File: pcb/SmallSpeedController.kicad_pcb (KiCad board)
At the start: 4 copper layers, 30.7 x 51.7 mm, 38 parts, among them J1 Conn_01x02_Socket, J10 Conn_01x03_Socket, J11 Conn_01x03_Socket, J2 Conn_01x02_Socket, J4 Conn_01x02_Socket, J5 Conn_01x04_Socket, J6 Conn_01x04_Socket, J9 Conn_01x03_Socket, SW2 TS-1088-AR02016, U2 AMS1117-3.3, U3 DRV8837DSGR, U4 DRV8837DSGR, U5 CH32V003FxUx

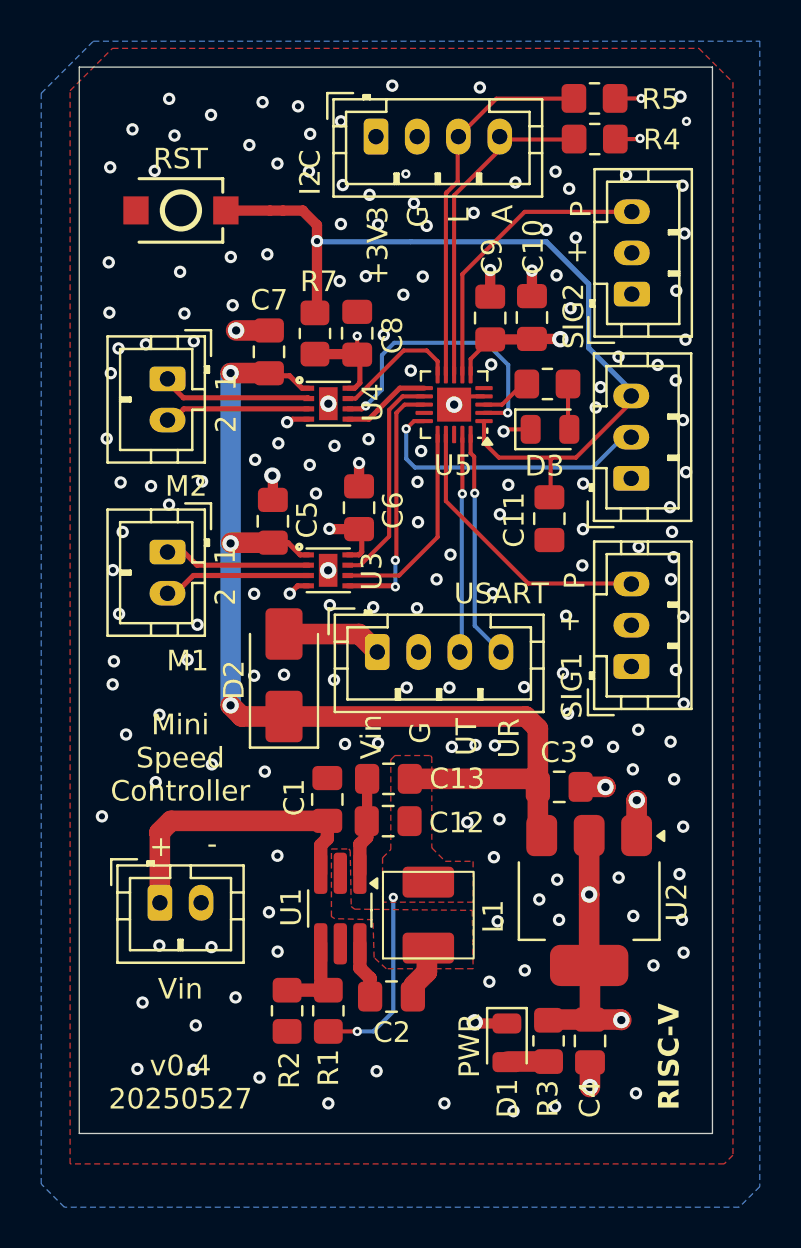
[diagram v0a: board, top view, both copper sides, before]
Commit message: pcb, sch: small cleanups for next fabrication round
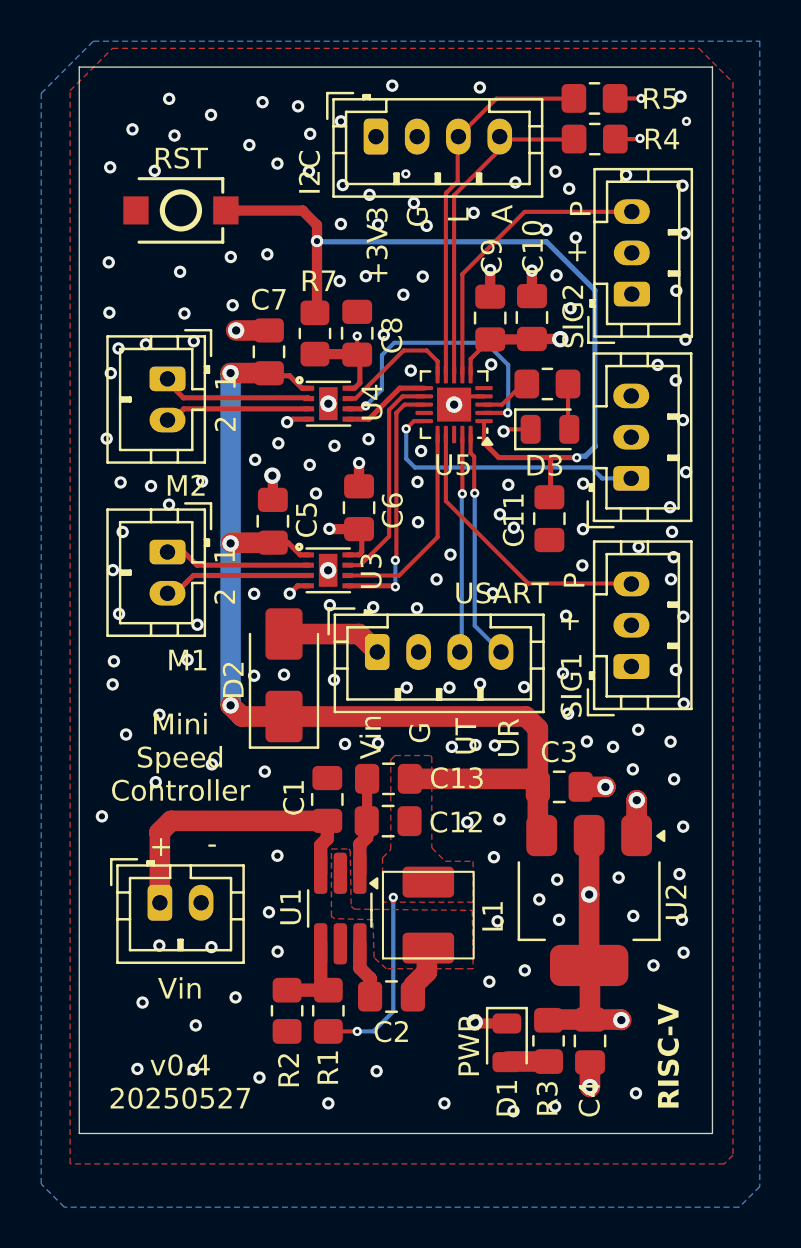
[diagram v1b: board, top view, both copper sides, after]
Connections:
- J11 pad 1: GND -> /SWDIO
- J11 pad 2: /SWDIO -> /+3V3
- J11 pad 3: /nRST -> GND
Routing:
- net /nRST: track 40.2 -> 39.3 mm, vias 1 -> 2
- net GND: vias 177 -> 176
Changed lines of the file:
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@@
 			(remove_unused_layers no)
 			(roundrect_rratio 0.208333)
-			(net 2 "GND")
+			(net 9 "/SWDIO")
 			(pinfunction "Pin_1")
 			(pintype "passive")
@@
 			(layers "*.Cu" "*.Mask")
 			(remove_unused_layers no)
-			(net 9 "/SWDIO")
+			(net 3 "/+3V3")
 			(pinfunction "Pin_2")
 			(pintype "passive")
@@
 			(layers "*.Cu" "*.Mask")
 			(remove_unused_layers no)
-			(net 4 "/nRST")
+			(net 2 "GND")
 			(pinfunction "Pin_3")
 			(pintype "passive")
@@
 	)
 	(via
-		(at 44.57 84.79)
-		(size 0.6)
-		(drill 0.3)
-		(layers "F.Cu" "B.Cu")
-		(free yes)
-		(net 2)
-	)
-	(via
 		(at 25.91 70.6)
 		(size 0.6)
@@
 	)
 	(via
+		(at 38.96 98.19)
+		(size 0.6)
+		(drill 0.3)
+		(layers "F.Cu" "B.Cu")
+		(free yes)
+		(net 2)
+	)
+	(via
 		(at 31.9 86.65)
 		(size 0.6)
@@
 	)
 	(via
-		(at 44.8 83.8)
+		(at 32.21 75.89)
 		(size 0.6)
 		(drill 0.3)
@@
 	)
 	(via
-		(at 32.21 75.89)
+		(at 21.02 73.14)
 		(size 0.6)
 		(drill 0.3)
@@
 	)
 	(via
-		(at 21.02 73.14)
+		(at 47.575 82.725)
 		(size 0.6)
 		(drill 0.3)
@@
 	)
 	(via
-		(at 47.575 82.725)
+		(at 40.6 90.62)
 		(size 0.6)
 		(drill 0.3)
@@
 	)
 	(via
-		(at 45.675 82.325)
-		(size 0.6)
-		(drill 0.3)
-		(layers "F.Cu" "B.Cu")
-		(free yes)
-		(net 2)
-	)
-	(via
 		(at 25.25 95.325)
 		(size 0.6)
@@
 	)
 	(segment
-		(start 43.61 87.22)
-		(end 46.205 84.625)
-		(width 0.2)
-		(layer "F.Cu")
-		(net 4)
-	)
-	(segment
 		(start 42.47 87.22)
 		(end 42.38 87.31)
@@
 		(start 39.15 86.5)
 		(end 39.87 87.22)
-		(width 0.2)
+		(width 0.25)
 		(layer "F.Cu")
 		(net 4)
 	)
 	(segment
-		(start 29.4 75.24)
-		(end 28.77 75.24)
+		(start 27.19 75.24)
+		(end 30.37 75.24)
 		(width 0.5)
 		(layer "F.Cu")
@@
 		(start 39.87 87.22)
 		(end 42.47 87.22)
-		(width 0.2)
+		(width 0.25)
 		(layer "F.Cu")
 		(net 4)
@@
 	)
 	(segment
-		(start 28.77 75.24)
-		(end 27.19 75.24)
-		(width 0.5)
-		(layer "F.Cu")
-		(net 4)
-	)
-	(segment
 		(start 42.38 87.31)
 		(end 42.38 89.1525)
-		(width 0.2)
+		(width 0.25)
 		(layer "F.Cu")
 		(net 4)
@@
 		(start 42.47 87.22)
 		(end 43.61 87.22)
-		(width 0.2)
+		(width 0.25)
 		(layer "F.Cu")
 		(net 4)
 	)
-	(segment
-		(start 30.37 75.24)
-		(end 29.4 75.24)
-		(width 0.5)
-		(layer "F.Cu")
+	(via
+		(at 43.65 87.225)
+		(size 0.45)
+		(drill 0.2)
+		(layers "F.Cu" "B.Cu")
 		(net 4)
 	)
@@
 	)
 	(segment
-		(start 46.525 84.2)
-		(end 44.225 81.9)
+		(start 44.07 87.15)
+		(end 44.55 86.67)
 		(width 0.25)
 		(layer "B.Cu")
@@
 	)
 	(segment
-		(start 31.08 76.75)
-		(end 35.6 76.75)
+		(start 43.725 87.15)
+		(end 44.07 87.15)
 		(width 0.25)
 		(layer "B.Cu")
@@
 	)
 	(segment
-		(start 44.225 81.9)
-		(end 44.225 78.8)
+		(start 44.53 86.65)
+		(end 44.53 79.105)
 		(width 0.25)
 		(layer "B.Cu")
@@
 	)
 	(segment
-		(start 44.225 78.8)
+		(start 43.65 87.225)
+		(end 43.725 87.15)
+		(width 0.25)
+		(layer "B.Cu")
+		(net 4)
+	)
+	(segment
+		(start 44.55 86.67)
+		(end 44.53 86.65)
+		(width 0.25)
+		(layer "B.Cu")
+		(net 4)
+	)
+	(segment
+		(start 44.53 79.105)
 		(end 42.175 76.75)
 		(width 0.25)
@@
 	(segment
 		(start 42.175 76.75)
-		(end 35.6 76.75)
+		(end 31.08 76.75)
 		(width 0.25)
 		(layer "B.Cu")
@@
 	)
 	(segment
-		(start 44.425 87.7)
-		(end 45.925 86.2)
+		(start 35.376 85.825)
+		(end 35.376 87.276)
 		(width 0.2)
 		(layer "B.Cu")
@@
 	)
 	(segment
-		(start 35.376 85.825)
-		(end 35.376 87.276)
+		(start 44.88 88.23)
+		(end 46.29 88.23)
 		(width 0.2)
 		(layer "B.Cu")
@@
 	)
 	(segment
-		(start 35.376 87.276)
-		(end 35.8 87.7)
+		(start 44.35 87.7)
+		(end 44.88 88.23)
 		(width 0.2)
 		(layer "B.Cu")
@@
 	(segment
 		(start 35.8 87.7)
-		(end 44.425 87.7)
+		(end 44.35 87.7)
+		(width 0.2)
+		(layer "B.Cu")
+		(net 9)
+	)
+	(segment
+		(start 35.376 87.276)
+		(end 35.8 87.7)
 		(width 0.2)
 		(layer "B.Cu")

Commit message: pcb: move silk prints around
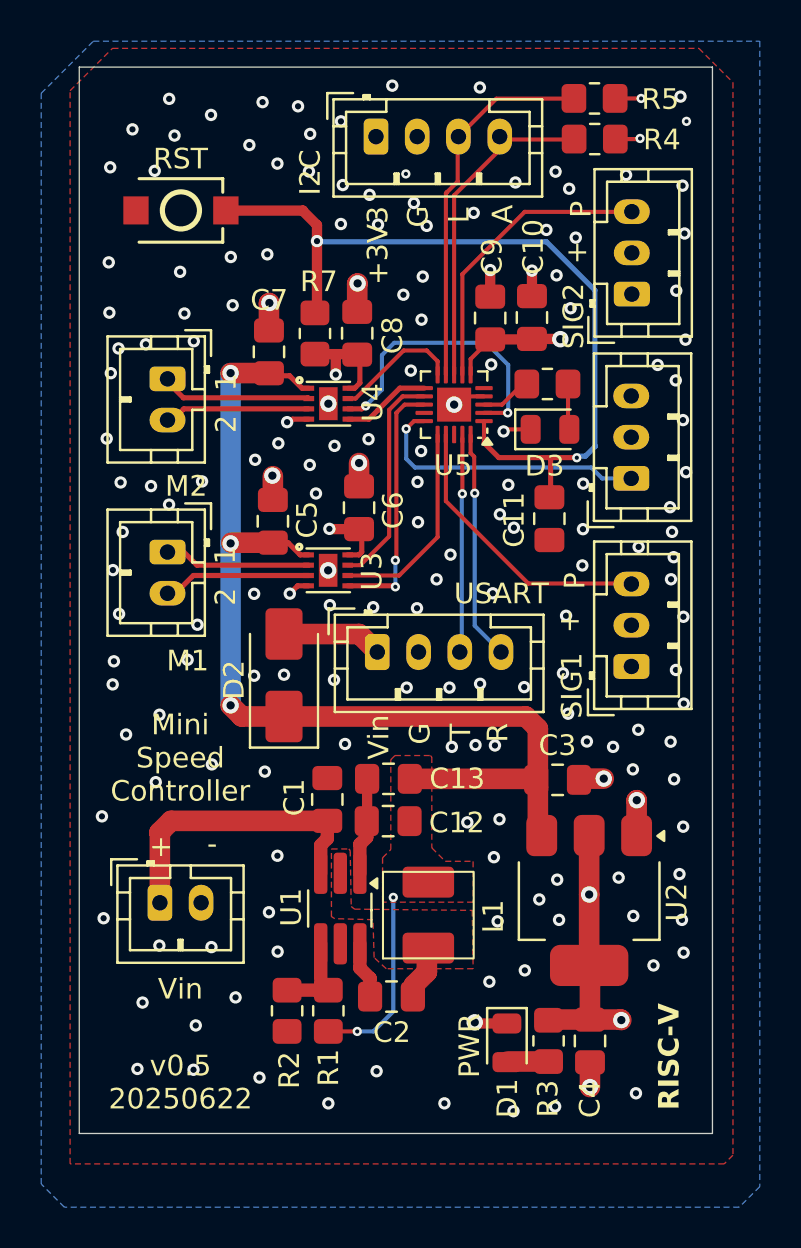
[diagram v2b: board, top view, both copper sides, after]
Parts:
- C11: value C -> 100nF
- U1: value ~ -> AP62300TWU
- moved C3 0.35 mm to (42.7, 102.8)
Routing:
- net GND: track 21.4 -> 22.5 mm, vias 176 -> 175
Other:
- board text added: "R"
- board text added: "T"
- board text added: "v0.5 20250622"
- board text removed: "UR"
- board text removed: "UT"
- board text removed: "v0.4 20250527"
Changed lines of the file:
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@@
 	(footprint "Capacitor_SMD:C_0805_2012Metric_Pad1.18x1.45mm_HandSolder"
 		(layer "F.Cu")
-		(at 42.8 103.19)
+		(at 42.72 102.85)
 		(descr "Capacitor SMD 0805 (2012 Metric), square (rectangular) end terminal, IPC-7351 nominal with elongated pad for handsoldering. (Body size source: IPC-SM-782 page 76, https://www.pcb-3d.com/wordpress/wp-content/uploads/ipc-sm-782a_amendment_1_and_2.pdf, https://docs.google.com/spreadsheets/d/1BsfQQcO9C6DZCsRaXUlFlo91Tg2WpOkGARC1WS5S8t0/edit?usp=sharing), generated with kicad-footprint-generator")
 		(tags "capacitor handsolder")
@@
 			)
 		)
-		(property "Value" "C"
+		(property "Value" "100nF"
 			(at 0 1.68 90)
 			(layer "F.Fab")
@@
 			)
 		)
-		(property "Value" "~"
+		(property "Value" "AP62300TWU"
 			(at 0 2.5 90)
 			(layer "F.Fab")
@@
 	)
 	(gr_text "G"
-		(at 36.65 101.1 90)
+		(at 36.63 101.14 90)
 		(layer "F.SilkS")
 		(effects
@@
 		)
 	)
-	(gr_text "UR"
-		(at 40.95 101.81 90)
+	(gr_text "R"
+		(at 40.4 101.04 90)
 		(layer "F.SilkS")
 		(effects
@@
 		)
 	)
-	(gr_text "v0.4\n20250527"
+	(gr_text "v0.5\n20250622"
 		(at 24.43 118.91 0)
 		(layer "F.SilkS")
@@
 		)
 	)
-	(gr_text "UT"
-		(at 38.89 101.69 90)
+	(gr_text "T"
+		(at 38.6 100.96 90)
 		(layer "F.SilkS")
 		(effects
@@
 	)
 	(gr_text "Vin"
-		(at 34.27 101.86 90)
+		(at 34.63 101.87 90)
 		(layer "F.SilkS")
 		(effects
@@
 		(start 33.09 88.6125)
 		(end 33.09 87.4825)
-		(width 0.5)
+		(width 1)
 		(layer "F.Cu")
 		(net 2)
@@
 	)
 	(segment
-		(start 43.8375 103.19)
-		(end 45.035 103.19)
+		(start 43.76125 102.79)
+		(end 44.95875 102.79)
 		(width 1)
 		(layer "F.Cu")
@@
 	)
 	(segment
-		(start 45.035 103.19)
-		(end 45.04 103.195)
+		(start 33 80.15)
+		(end 33 78.79)
 		(width 1)
 		(layer "F.Cu")
@@
 	)
 	(segment
+		(start 28.72 81.0525)
+		(end 28.72 79.74)
+		(width 1)
+		(layer "F.Cu")
+		(net 2)
+	)
+	(segment
 		(start 33.13 105.97)
 		(end 33.13 107.38)
@@
 		(start 28.91 89.27)
 		(end 28.91 88.12)
-		(width 0.5)
+		(width 1)
 		(layer "F.Cu")
 		(net 2)
 	)
 	(segment
-		(start 28.72 81.0525)
-		(end 27.1275 81.0525)
+		(start 28.72 79.74)
+		(end 28.74 79.72)
+		(width 1)
+		(layer "F.Cu")
+		(net 2)
+	)
+	(segment
+		(start 33 78.79)
+		(end 33.02 78.77)
 		(width 1)
 		(layer "F.Cu")
@@
 	(via
 		(at 33.09 87.4825)
-		(size 0.6)
-		(drill 0.3)
+		(size 0.8)
+		(drill 0.4)
 		(layers "F.Cu" "B.Cu")
 		(net 2)
@@
 	)
 	(via
-		(at 27.1275 81.0525)
+		(at 28.74 79.72)
 		(size 0.8)
 		(drill 0.4)
@@
 	)
 	(via
-		(at 33.42 78.42)
-		(size 0.6)
-		(drill 0.3)
-		(layers "F.Cu" "B.Cu")
-		(free yes)
-		(net 2)
-	)
-	(via
 		(at 27.1 113.4)
 		(size 0.6)
@@
 	)
 	(via
-		(at 45.04 103.195)
+		(at 44.95875 102.79)
 		(size 0.8)
 		(drill 0.4)
@@
 	)
 	(via
-		(at 34.01 101.07)
+		(at 20.7 109.56)
 		(size 0.6)
 		(drill 0.3)
@@
 	)
 	(via
-		(at 32.15 78.66)
-		(size 0.6)
-		(drill 0.3)
-		(layers "F.Cu" "B.Cu")
-		(free yes)
-		(net 2)
-	)
-	(via
 		(at 37.475 98.375)
 		(size 0.6)
@@
 	)
 	(via
+		(at 33.02 78.77)
+		(size 0.8)
+		(drill 0.4)
+		(layers "F.Cu" "B.Cu")
+		(net 2)
+	)
+	(via
 		(at 40.6 90.62)
 		(size 0.6)
@@
 	)
 	(via
-		(at 34.29 81.27)
+		(at 36.12 80.53)
 		(size 0.6)
 		(drill 0.3)
@@
 	)
 	(segment
-		(start 30.95 82.2)
+		(start 31.96 82.25)
+		(end 32.01 82.2)
+		(width 0.5)
+		(layer "F.Cu")
+		(net 3)
+	)
+	(segment
+		(start 32.01 82.2)
 		(end 32.975 82.2)
 		(width 0.5)
@@
 	)
 	(segment
+		(start 30.95 82.2)
+		(end 32.01 82.2)
+		(width 0.5)
+		(layer "F.Cu")
+		(net 3)
+	)
+	(segment
 		(start 32.54 91.9375)
 		(end 33.0825 91.9375)
@@
 	)
 	(segment
-		(start 33 81.325)
-		(end 33 82.225)
-		(width 0.2)
-		(layer "F.Cu")
-		(net 3)
-	)
-	(segment
 		(start 44.25 108.41)
 		(end 44.25 111.85)
@@
 		(net 3)
 	)
+	(segment
+		(start 31.96 83.19)
+		(end 31.96 82.25)
+		(width 0.5)
+		(layer "F.Cu")
+		(net 3)
+	)
 	(via
 		(at 45.81 114.5)
@@
 	)
 	(via
-		(at 33 81.325)
-		(size 0.45)
-		(drill 0.2)
-		(layers "F.Cu" "B.Cu")
-		(net 3)
-	)
-	(via
 		(at 46.77 69.8)
 		(size 0.45)
@@
 		(net 3)
 	)
+	(via
+		(at 31.96 83.19)
+		(size 0.6)
+		(drill 0.3)
+		(layers "F.Cu" "B.Cu")
+		(net 3)
+	)
 	(segment
 		(start 31.05 76.72)
@@
 	)
 	(segment
-		(start 38.699324 88.946461)
-		(end 38.675 88.922137)
+		(start 38.675 87.175)
+		(end 38.5 87)
 		(width 0.2)
 		(layer "F.Cu")
@@
 	)
 	(segment
-		(start 38.675 87.175)
-		(end 38.5 87)
+		(start 38.675 88.922137)
+		(end 38.675 87.175)
 		(width 0.2)
 		(layer "F.Cu")
@@
 	)
 	(segment
-		(start 38.5 87)
-		(end 38.5 86.125)
+		(start 38.699324 88.946461)
+		(end 38.675 88.922137)
 		(width 0.2)
 		(layer "F.Cu")
@@
 	)
 	(segment
-		(start 38.675 88.922137)
-		(end 38.675 87.175)
+		(start 38.5 87)
+		(end 38.5 86.125)
 		(width 0.2)
 		(layer "F.Cu")
@@
 	)
 	(segment
-		(start 38.7 95.375)
-		(end 39.975 96.65)
+		(start 38.771458 88.946461)
+		(end 38.7 89.017919)
 		(width 0.2)
 		(layer "B.Cu")
@@
 	)
 	(segment
-		(start 38.699324 88.946461)
-		(end 38.771458 88.946461)
+		(start 38.7 89.017919)
+		(end 38.7 95.375)
 		(width 0.2)
 		(layer "B.Cu")
@@
 	)
 	(segment
-		(start 38.771458 88.946461)
-		(end 38.7 89.017919)
+		(start 38.7 95.375)
+		(end 39.975 96.65)
 		(width 0.2)
 		(layer "B.Cu")
@@
 	)
 	(segment
-		(start 38.7 89.017919)
-		(end 38.7 95.375)
+		(start 38.699324 88.946461)
+		(end 38.771458 88.946461)
 		(width 0.2)
 		(layer "B.Cu")

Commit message: pcb: give 3v3 on the UART connector and get rid of diode
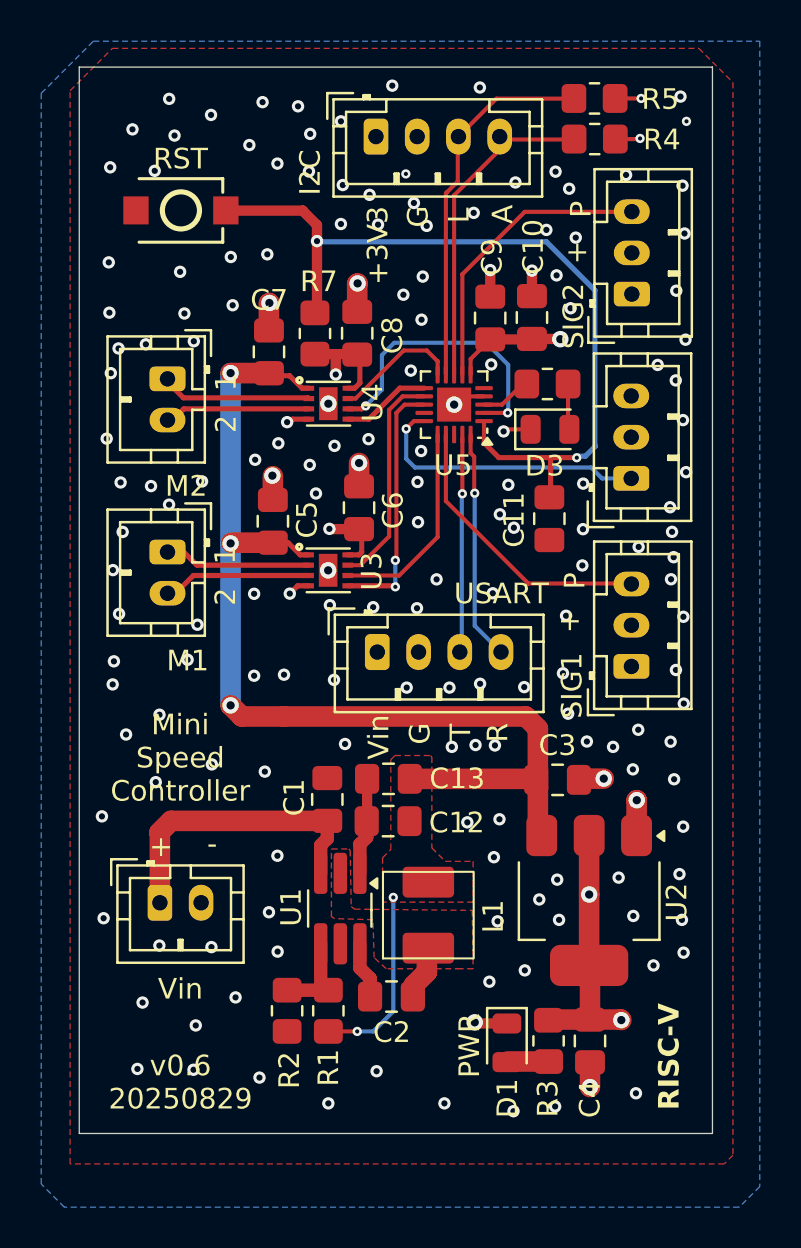
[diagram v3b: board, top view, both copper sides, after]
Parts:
- removed D2: SS26, Diode_SMD:D_SMA
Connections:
- J6 pad 1: Net-(D2-A) -> /+3V3
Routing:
- net Net-(D2-A): track 4.89 -> 0.00 mm
- net GND: vias 175 -> 174
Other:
- board text added: "v0.6 20250829"
- board text removed: "v0.5 20250622"
